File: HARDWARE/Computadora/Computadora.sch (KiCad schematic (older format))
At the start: 45 parts, among them IC1 ATMEGA328-P, J1 DB9, K1 AUX_PINS, P1 MOTORS PWM OUTPUT, P2 CONN_2, P3 CONN_SENSORES, Q1 BS170, Q2 BS170, SW1 RESET, U1 MAX232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

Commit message: Se termina primera version del pcb. yeah!
Signed-off-by: Gonzalo Nahuel Vaca <vacagonzalo@gmail.com>
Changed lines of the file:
@@
 LIBS:contrib
 LIBS:valves
+LIBS:Computadora-cache
 EELAYER 27 0
 EELAYER END
@@
 Sheet 1 1
 Title "Computadora a bordo - Cuadricoptero"
-Date "14 jul 2015"
+Date "22 jul 2015"
 Rev "5"
 Comp "UNLAM"
@@
 L PWR_FLAG #FLG4
 U 1 1 55A55072
-P 3700 1000
-F 0 "#FLG4" H 3700 1095 30  0001 C CNN
-F 1 "PWR_FLAG" H 3700 1180 30  0000 C CNN
-F 2 "" H 3700 1000 60  0000 C CNN
-F 3 "" H 3700 1000 60  0000 C CNN
-	1    3700 1000
+P 3700 950
+F 0 "#FLG4" H 3700 1045 30  0001 C CNN
+F 1 "PWR_FLAG" H 3700 1130 30  0000 C CNN
+F 2 "" H 3700 950 60  0000 C CNN
+F 3 "" H 3700 950 60  0000 C CNN
+	1    3700 950
 	1    0    0    -1
 $EndComp
@@
 	3900 1000 3900 950
 Wire Wire Line
-	3700 1250 3700 1000
+	3700 950  3700 1250
 Wire Wire Line
 	3700 1750 3700 2050

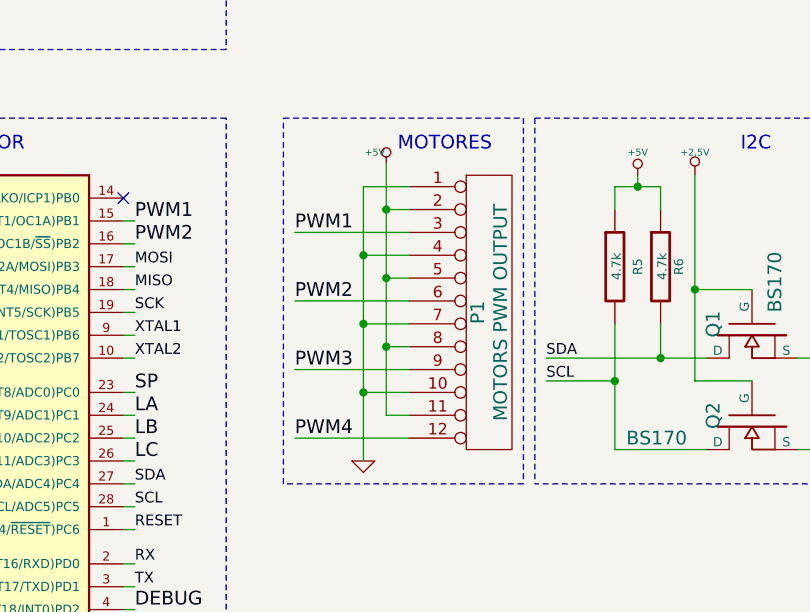
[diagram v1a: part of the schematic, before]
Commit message: Se hace una nueva placa y circuito esquemático separando los motores
Signed-off-by: Gonzalo Nahuel Vaca <vacagonzalo@gmail.com>
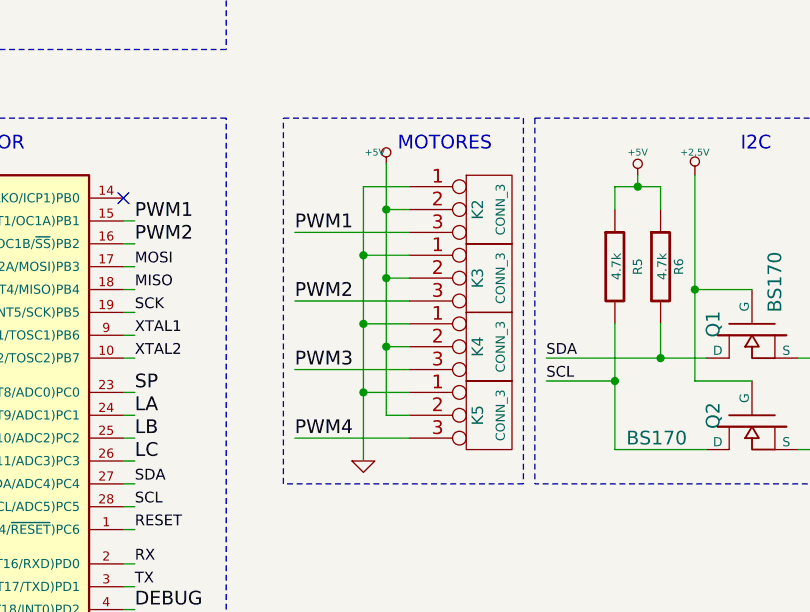
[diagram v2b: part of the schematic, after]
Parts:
- removed P1: MOTORS PWM OUTPUT, symbol CONN_12
- added K2, K3, K4, K5: CONN_3, symbol CONN_3
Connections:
- net +5V: now also K2.2 (PM), K3.2 (PM), K4.2 (PM), K5.2 (PM)
- net GND: now also K2.1 (P1), K3.1 (P1), K4.1 (P1), K5.1 (P1)
- net PWM1: now also K2.3 (P3)
- net PWM2: now also K3.3 (P3)
- net PWM3: now also K4.3 (P3)
- net PWM4: now also K5.3 (P3)
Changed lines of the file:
@@
 Sheet 1 1
 Title "Computadora a bordo - Cuadricoptero"
-Date "22 jul 2015"
-Rev "5"
+Date "23 jul 2015"
+Rev "6"
 Comp "UNLAM"
 Comment1 ""
@@
 Text Label 6400 4500 0    47   ~ 0
 TX
-$Comp
-L CONN_12 P1
-U 1 1 54530F3A
-P 7950 3300
-F 0 "P1" V 7900 3300 60  0000 C CNN
-F 1 "MOTORS PWM OUTPUT" V 8000 3300 60  0000 C CNN
-F 2 "" H 7950 3300 60  0000 C CNN
-F 3 "" H 7950 3300 60  0000 C CNN
-	1    7950 3300
-	1    0    0    -1
-$EndComp
 $Comp
 L +5V #PWR29
@@
 Wire Wire Line
 	7500 2650 7500 3750
-Wire Wire Line
-	7500 2850 7600 2850
-Wire Wire Line
-	7500 3150 7600 3150
 Connection ~ 7500 2850
-Wire Wire Line
-	7500 3450 7600 3450
 Connection ~ 7500 3150
-Wire Wire Line
-	7500 3750 7600 3750
 Connection ~ 7500 3450
 Wire Wire Line
-	7400 3650 7600 3650
-Wire Wire Line
 	7400 2750 7400 3950
-Wire Wire Line
-	7600 3350 7400 3350
 Connection ~ 7400 3650
-Wire Wire Line
-	7600 3050 7400 3050
 Connection ~ 7400 3350
-Wire Wire Line
-	7600 2750 7400 2750
 Connection ~ 7400 3050
 Wire Wire Line
@@
 	6400 3000 6350 3000
 Wire Wire Line
-	7100 2950 7600 2950
-Wire Wire Line
-	7100 3250 7600 3250
-Wire Wire Line
-	7100 3550 7600 3550
-Wire Wire Line
-	7100 3850 7600 3850
-Wire Wire Line
 	6400 3100 6350 3100
 Wire Wire Line
@@
 Text Notes 10050 2650 3    60   ~ 0
 Macho
+$Comp
+L CONN_3 K2
+U 1 1 55B038EF
+P 7950 2850
+F 0 "K2" V 7900 2850 50  0000 C CNN
+F 1 "CONN_3" V 8000 2850 40  0000 C CNN
+F 2 "" H 7950 2850 60  0000 C CNN
+F 3 "" H 7950 2850 60  0000 C CNN
+	1    7950 2850
+	1    0    0    -1
+$EndComp
+$Comp
+L CONN_3 K3
+U 1 1 55B038FE
+P 7950 3150
+F 0 "K3" V 7900 3150 50  0000 C CNN
+F 1 "CONN_3" V 8000 3150 40  0000 C CNN
+F 2 "" H 7950 3150 60  0000 C CNN
+F 3 "" H 7950 3150 60  0000 C CNN
+	1    7950 3150
+	1    0    0    -1
+$EndComp
+$Comp
+L CONN_3 K4
+U 1 1 55B0390D
+P 7950 3450
+F 0 "K4" V 7900 3450 50  0000 C CNN
+F 1 "CONN_3" V 8000 3450 40  0000 C CNN
+F 2 "" H 7950 3450 60  0000 C CNN
+F 3 "" H 7950 3450 60  0000 C CNN
+	1    7950 3450
+	1    0    0    -1
+$EndComp
+$Comp
+L CONN_3 K5
+U 1 1 55B0391C
+P 7950 3750
+F 0 "K5" V 7900 3750 50  0000 C CNN
+F 1 "CONN_3" V 8000 3750 40  0000 C CNN
+F 2 "" H 7950 3750 60  0000 C CNN
+F 3 "" H 7950 3750 60  0000 C CNN
+	1    7950 3750
+	1    0    0    -1
+$EndComp
+Wire Wire Line
+	7600 3850 7100 3850
+Wire Wire Line
+	7100 3550 7600 3550
+Wire Wire Line
+	7100 3250 7600 3250
+Wire Wire Line
+	7100 2950 7600 2950
+Wire Wire Line
+	7600 2750 7400 2750
+Wire Wire Line
+	7400 3050 7600 3050
+Wire Wire Line
+	7600 2850 7500 2850
+Wire Wire Line
+	7600 3150 7500 3150
+Wire Wire Line
+	7600 3350 7400 3350
+Wire Wire Line
+	7600 3450 7500 3450
+Wire Wire Line
+	7600 3650 7400 3650
+Wire Wire Line
+	7500 3750 7600 3750
 $EndSCHEMATC
